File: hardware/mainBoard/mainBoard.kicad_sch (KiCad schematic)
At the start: 19 parts, among them J1 UARTDebug, J2 LeftKeyConnector, J3 DisplayConnector, J4 RightKeyConnector, J5 EncoderConnector, U1 MCP4728-E_UN

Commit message: add led headers to main board
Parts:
- removed J5: EncoderConnector, Connector_JST:JST_XH_B4B-XH-A_1x04_P2.50mm_Vertical, symbol Connector_Generic:Conn_01x04
- added J4: LEDHeader, Connector_JST:JST_XH_B3B-XH-A_1x03_P2.50mm_Vertical, symbol Connector_Generic:Conn_01x03
- added J6: EncoderConnector, Connector_JST:JST_XH_B5B-XH-A_1x05_P2.50mm_Vertical, symbol Connector_Generic:Conn_01x05
- renumbered J4 to J5
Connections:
- net +5V: now also J4.3 (Pin_3)
- net GND: now also J4.1 (Pin_1), J6.5 (Pin_5)
- net at A1.20 (GPIO15): now also J4.2 (Pin_2)
- net at A1.26 (GPIO20): now also J6.1 (Pin_1)
- net at A1.27 (GPIO21): now also J6.2 (Pin_2)
- net at A1.29 (GPIO22): now also J6.3 (Pin_3)
- net at A1.31 (GPIO26_ADC0): now also J6.4 (Pin_4)
- no-connect marks 10 -> 9

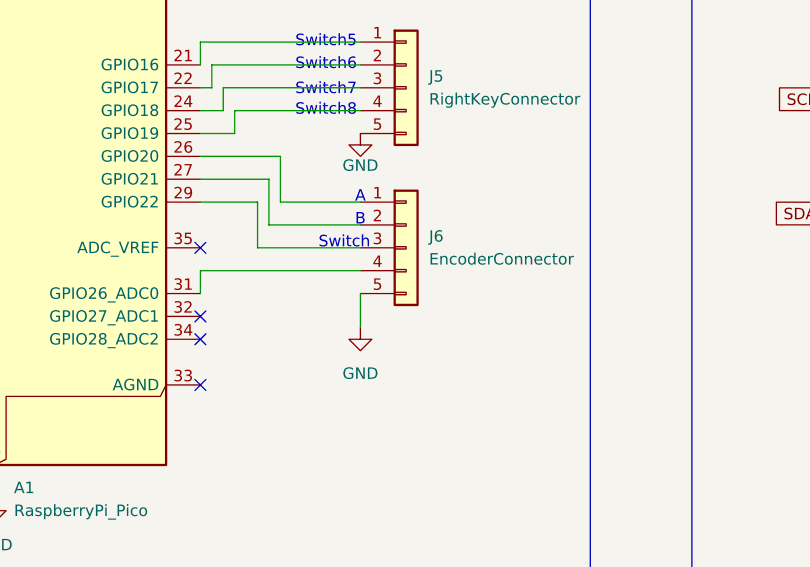
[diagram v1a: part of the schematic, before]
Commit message: add led header to pcb
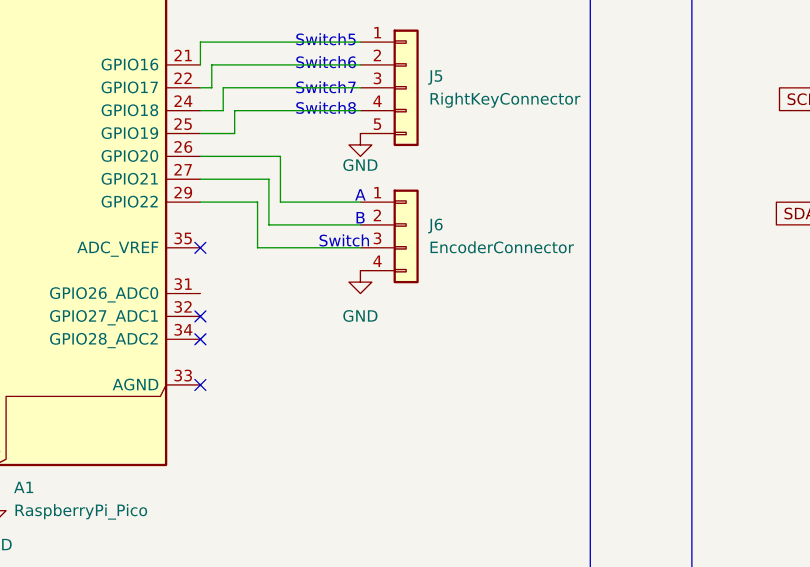
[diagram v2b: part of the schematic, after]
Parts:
- removed J6: EncoderConnector, Connector_JST:JST_XH_B5B-XH-A_1x05_P2.50mm_Vertical, symbol Connector_Generic:Conn_01x05
- added J6: EncoderConnector, Connector_JST:JST_XH_B4B-XH-A_1x04_P2.50mm_Vertical, symbol Connector_Generic:Conn_01x04
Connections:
- net GND: now also J6.4 (Pin_4)
- net at A1.26 (GPIO20): now also J6.1 (Pin_1)
- net at A1.27 (GPIO21): now also J6.2 (Pin_2)
- net at A1.29 (GPIO22): now also J6.3 (Pin_3)
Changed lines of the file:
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@@
 	(wire
 		(pts
-			(xy 128.27 73.66) (xy 110.49 73.66)
-		)
-		(stroke
-			(width 0)
-			(type default)
-		)
-	)
-	(wire
-		(pts
 			(xy 185.42 50.8) (xy 185.42 54.61)
 		)
@@
 	(wire
 		(pts
-			(xy 128.27 76.2) (xy 128.27 80.01)
-		)
-		(stroke
-			(width 0)
-			(type default)
-		)
-	)
-	(wire
-		(pts
 			(xy 39.37 95.25) (xy 38.1 95.25)
 		)
@@
 	(wire
 		(pts
-			(xy 110.49 73.66) (xy 110.49 76.2)
-		)
-		(stroke
-			(width 0)
-			(type default)
-		)
-	)
-	(wire
-		(pts
 			(xy 118.11 63.5) (xy 110.49 63.5)
 		)
@@
 	)
 	(symbol
+		(lib_id "Connector_Generic:Conn_01x04")
+		(at 133.35 68.58 0)
+		(unit 1)
+		(body_style 1)
+		(exclude_from_sim no)
+		(in_bom yes)
+		(on_board yes)
+		(in_pos_files yes)
+		(dnp no)
+		(fields_autoplaced yes)
+		(property "Reference" "J6"
+			(at 135.89 68.5799 0)
+			(show_name no)
+			(do_not_autoplace no)
+			(effects
+				(font
+					(size 1.27 1.27)
+				)
+				(justify left)
+			)
+		)
+		(property "Value" "EncoderConnector"
+			(at 135.89 71.1199 0)
+			(show_name no)
+			(do_not_autoplace no)
+			(effects
+				(font
+					(size 1.27 1.27)
+				)
+				(justify left)
+			)
+		)
+		(property "Footprint" "Connector_JST:JST_XH_B4B-XH-A_1x04_P2.50mm_Vertical"
+			(at 133.35 68.58 0)
+			(hide yes)
+			(show_name no)
+			(do_not_autoplace no)
+			(effects
+				(font
+					(size 1.27 1.27)
+				)
+			)
+		)
+		(property "Datasheet" ""
+			(at 133.35 68.58 0)
+			(hide yes)
+			(show_name no)
+			(do_not_autoplace no)
+			(effects
+				(font
+					(size 1.27 1.27)
+				)
+			)
+		)
+		(property "Description" "Generic connector, single row, 01x04, script generated (kicad-library-utils/schlib/autogen/connector/)"
+			(at 133.35 68.58 0)
+			(hide yes)
+			(show_name no)
+			(do_not_autoplace no)
+			(effects
+				(font
+					(size 1.27 1.27)
+				)
+			)
+		)
+		(pin "4"
+		)
+		(pin "1"
+		)
+		(pin "3"
+		)
+		(pin "2"
+		)
+		(instances
+			(project "mainBoard"
+				(path "/be2e610a-0da0-4417-ae24-40d589f4bf40"
+					(reference "J6")
+					(unit 1)
+				)
+			)
+		)
+	)
+	(symbol
 		(lib_id "power:GND")
 		(at 87.63 99.06 0)
@@
 	(symbol
 		(lib_id "power:GND")
-		(at 128.27 80.01 0)
+		(at 128.27 73.66 0)
 		(unit 1)
 		(body_style 1)
@@
 		(fields_autoplaced yes)
 		(property "Reference" "#PWR013"
-			(at 128.27 86.36 0)
+			(at 128.27 80.01 0)
 			(hide yes)
 			(show_name no)
@@
 		)
 		(property "Value" "GND"
-			(at 128.27 85.09 0)
+			(at 128.27 78.74 0)
 			(show_name no)
 			(do_not_autoplace no)
@@
 		)
 		(property "Footprint" ""
-			(at 128.27 80.01 0)
+			(at 128.27 73.66 0)
 			(hide yes)
 			(show_name no)
@@
 		)
 		(property "Datasheet" ""
-			(at 128.27 80.01 0)
+			(at 128.27 73.66 0)
 			(hide yes)
 			(show_name no)
@@
 		)
 		(property "Description" "Power symbol creates a global label with name \"GND\" , ground"
-			(at 128.27 80.01 0)
+			(at 128.27 73.66 0)
 			(hide yes)
 			(show_name no)
@@
 					(unit 1)
 				)
-			)
-		)
-	)
-	(symbol
-		(lib_id "Connector_Generic:Conn_01x05")
-		(at 133.35 71.12 0)
-		(unit 1)
-		(body_style 1)
-		(exclude_from_sim no)
-		(in_bom yes)
-		(on_board yes)
-		(in_pos_files yes)
-		(dnp no)
-		(fields_autoplaced yes)
-		(property "Reference" "J6"
-			(at 135.89 69.8499 0)
-			(show_name no)
-			(do_not_autoplace no)
-			(effects
-				(font
-					(size 1.27 1.27)
-				)
-				(justify left)
-			)
-		)
-		(property "Value" "EncoderConnector"
-			(at 135.89 72.3899 0)
-			(show_name no)
-			(do_not_autoplace no)
-			(effects
-				(font
-					(size 1.27 1.27)
-				)
-				(justify left)
-			)
-		)
-		(property "Footprint" "Connector_JST:JST_XH_B5B-XH-A_1x05_P2.50mm_Vertical"
-			(at 133.35 71.12 0)
-			(hide yes)
-			(show_name no)
-			(do_not_autoplace no)
-			(effects
-				(font
-					(size 1.27 1.27)
-				)
-			)
-		)
-		(property "Datasheet" ""
-			(at 133.35 71.12 0)
-			(hide yes)
-			(show_name no)
-			(do_not_autoplace no)
-			(effects
-				(font
-					(size 1.27 1.27)
-				)
-			)
-		)
-		(property "Description" "Generic connector, single row, 01x05, script generated (kicad-library-utils/schlib/autogen/connector/)"
-			(at 133.35 71.12 0)
-			(hide yes)
-			(show_name no)
-			(do_not_autoplace no)
-			(effects
-				(font
-					(size 1.27 1.27)
-				)
-			)
-		)
-		(pin "1"
-		)
-		(pin "5"
-		)
-		(pin "4"
-		)
-		(pin "3"
-		)
-		(pin "2"
-		)
-		(instances
-			(project "mainBoard"
-				(path "/be2e610a-0da0-4417-ae24-40d589f4bf40"
-					(reference "J6")
-					(unit 1)
-				)

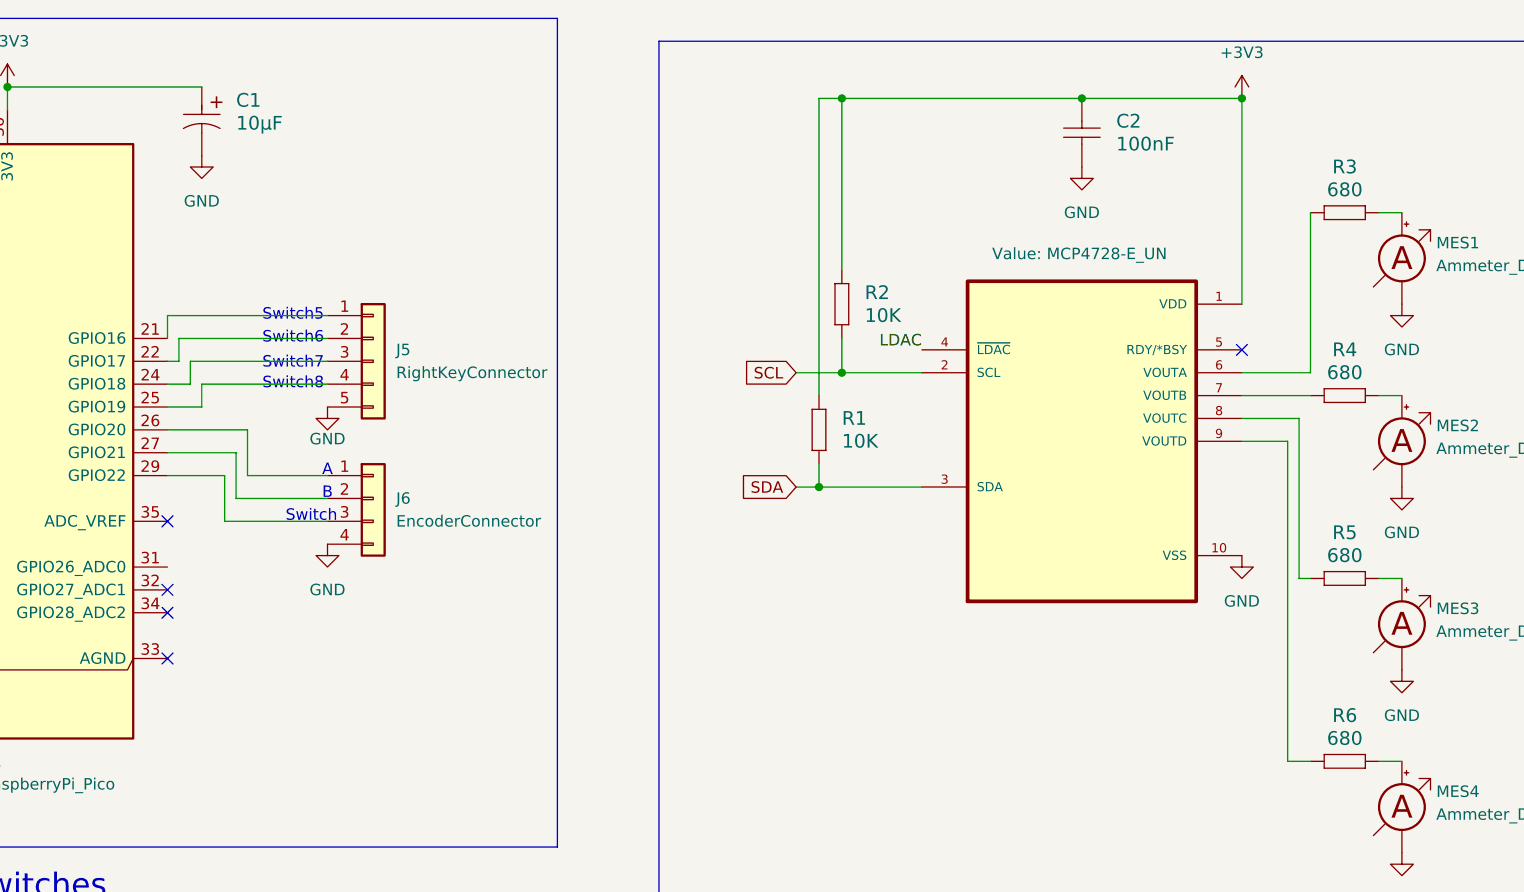
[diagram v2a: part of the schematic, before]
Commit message: update mainboard to use resistor array
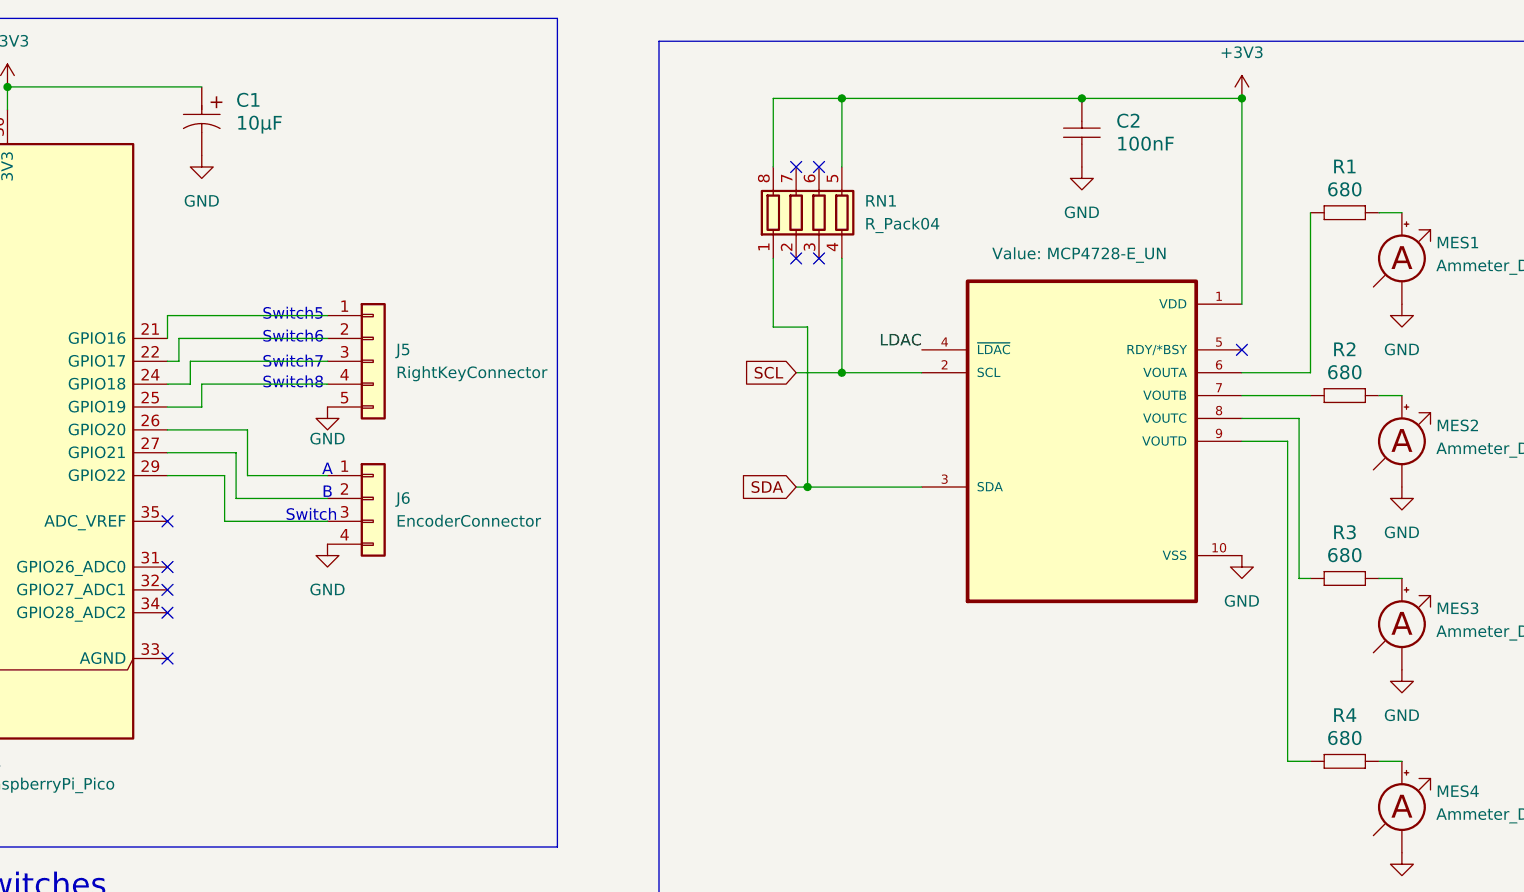
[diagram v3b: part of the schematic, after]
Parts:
- removed R1, R2: 10K, Resistor_SMD:R_1206_3216Metric_Pad1.30x1.75mm_HandSolder, symbol Resistors:Resistor
- added RN1: R_Pack04, Resistor_SMD:R_Array_Concave_4x0603, symbol Device:R_Pack04
- A1: LCSC Part # (none) -> C42924268; Price (none) -> $6.0306
- C1: LCSC Part # (none) -> C1952719; Price (none) -> $0.716
- C2: LCSC Part # (none) -> C1945; Price (none) -> $0.0333
- J1, J6: LCSC Part # (none) -> C144395; Price (none) -> $0.0574
- J2, J5: LCSC Part # (none) -> C157991; Price (none) -> $0.0878
- J3: LCSC Part # (none) -> C492407; Price (none) -> $0.0456
- J4: LCSC Part # (none) -> C144394; Price (none) -> $0.0543
- MES1, MES2, MES3, MES4: LCSC Part # (none) -> C158012; Price (none) -> $0.0405
- R1: renamed from R3; LCSC Part # (none) -> C137240; Price (none) -> $0.0066
- R2: renamed from R4; LCSC Part # (none) -> C137240; Price (none) -> $0.0066
- R3: renamed from R5; LCSC Part # (none) -> C137240; Price (none) -> $0.0066
- R4: renamed from R6; LCSC Part # (none) -> C137240; Price (none) -> $0.0066
- U1: LCSC Part # (none) -> C108207; Price None -> $2.5177
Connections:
- net +3V3: now also RN1.5 (R4.2), RN1.8 (R1.2)
- net SCL: now also RN1.4 (R4.1)
- net SDA: now also RN1.1 (R1.1)
- no-connect marks 9 -> 14

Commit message: add production files
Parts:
- RN1: value R_Pack04 -> 10K; LCSC Part # (none) -> C29718; Price (none) -> $0.0149
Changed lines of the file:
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@@
 			)
 		)
-		(property "Value" "R_Pack04"
+		(property "Value" "10K"
 			(at 187.96 38.0999 0)
 			(show_name no)
@@
 			(at 182.88 36.83 0)
 			(hide yes)
+			(show_name no)
+			(do_not_autoplace no)
+			(effects
+				(font
+					(size 1.27 1.27)
+				)
+			)
+		)
+		(property "LCSC Part #" "C29718"
+			(at 182.88 36.83 0)
+			(hide yes)
+			(show_name no)
+			(do_not_autoplace no)
+			(effects
+				(font
+					(size 1.27 1.27)
+				)
+			)
+		)
+		(property "Price" " $0.0149 "
+			(at 182.88 36.83 0)
+			(hide yes)

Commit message: update BOM to change capacitor + new gerbers + update the production files
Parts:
- C1: LCSC Part # C1952719 -> C1958016; Price $0.716 -> $ 0.2239
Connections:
- no-connect marks 14 -> 15
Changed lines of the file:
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@@
 	)
 	(no_connect
+		(at 177.8 35.56)
+	)
+	(no_connect
 		(at 110.49 76.2)
 	)
@@
 			)
 		)
-		(property "LCSC Part #" "C1952719"
+		(property "LCSC Part #" "C1958016"
 			(at 114.3 22.86 90)
 			(hide yes)
@@
 			)
 		)
-		(property "Price" " $0.716 "
+		(property "Price" "$ 0.2239"
 			(at 114.3 22.86 90)
 			(hide yes)

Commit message: update BOM.csv
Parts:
- C1: LCSC Part # C1958016 -> C7171; Price $ 0.2239 -> $0.1903
- C2: LCSC Part # C1945 -> C24497; Price $0.0333 -> $0.0259
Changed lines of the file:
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@@
 			)
 		)
-		(property "LCSC Part #" "C1945"
+		(property "LCSC Part #" "C24497"
 			(at 212.09 24.13 90)
 			(hide yes)
@@
 			)
 		)
-		(property "Price" " $0.0333 "
+		(property "Price" "$0.0259"
 			(at 212.09 24.13 90)
 			(hide yes)
@@
 			)
 		)
-		(property "LCSC Part #" "C1958016"
+		(property "LCSC Part #" " C7171 "
 			(at 114.3 22.86 90)
 			(hide yes)
@@
 			)
 		)
-		(property "Price" "$ 0.2239"
+		(property "Price" " $0.1903 "
 			(at 114.3 22.86 90)
 			(hide yes)

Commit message: update resistor size
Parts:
- R1, R2, R3, R4: value 680 -> 665; LCSC Part # C137240 -> C54532953; Price $0.0066 -> $0.0059
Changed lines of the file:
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@@
 			)
 		)
-		(property "Value" "680"
+		(property "Value" "665"
 			(at 241.3 95.25 0)
 			(show_name no)
@@
 			)
 		)
-		(property "LCSC Part #" "C137240"
+		(property "LCSC Part #" "C54532953"
 			(at 237.49 97.79 0)
 			(hide yes)
@@
 			)
 		)
-		(property "Price" " $0.0066 "
+		(property "Price" " $0.0059 "
 			(at 237.49 97.79 0)
 			(hide yes)
@@
 			)
 		)
-		(property "Value" "680"
+		(property "Value" "665"
 			(at 241.3 54.61 0)
 			(show_name no)
@@
 			)
 		)
-		(property "LCSC Part #" "C137240"
+		(property "LCSC Part #" "C54532953"
 			(at 237.49 57.15 0)
 			(hide yes)
@@
 			)
 		)
-		(property "Price" " $0.0066 "
+		(property "Price" " $0.0059 "
 			(at 237.49 57.15 0)
 			(hide yes)
@@
 			)
 		)
-		(property "Value" "680"
+		(property "Value" "665"
 			(at 241.3 74.93 0)
 			(show_name no)
@@
 			)
 		)
-		(property "LCSC Part #" "C137240"
+		(property "LCSC Part #" "C54532953"
 			(at 237.49 77.47 0)
 			(hide yes)
@@
 			)
 		)
-		(property "Price" " $0.0066 "
+		(property "Price" " $0.0059 "
 			(at 237.49 77.47 0)
 			(hide yes)
@@
 			)
 		)
-		(property "Value" "680"
+		(property "Value" "665"
 			(at 241.3 34.29 0)
 			(show_name no)
@@
 			)
 		)
-		(property "LCSC Part #" "C137240"
+		(property "LCSC Part #" "C54532953"
 			(at 237.49 36.83 0)
 			(hide yes)
@@
 			)
 		)
-		(property "Price" " $0.0066 "
+		(property "Price" " $0.0059 "
 			(at 237.49 36.83 0)
 			(hide yes)
